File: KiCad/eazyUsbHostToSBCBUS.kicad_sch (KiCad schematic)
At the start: 23 parts, among them J1 SBC-BUS, J2 KBD_JP, J3 SERIAL, Q1 2N7000, U2 74HC04

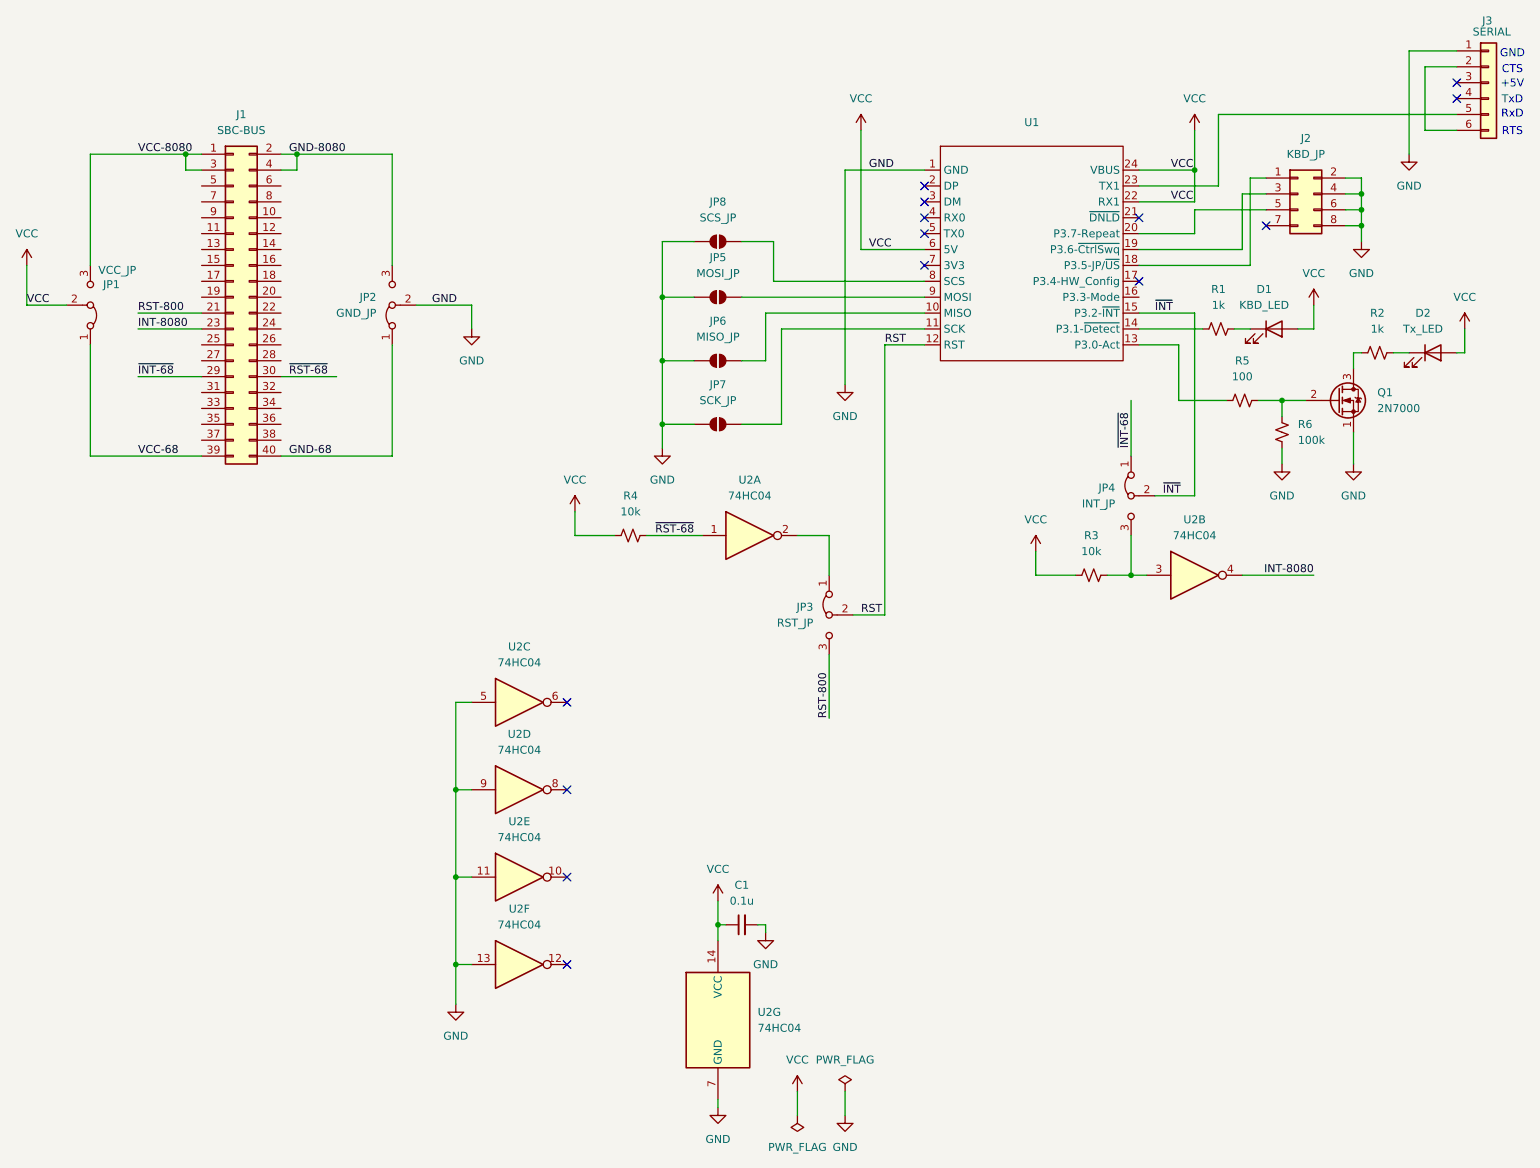
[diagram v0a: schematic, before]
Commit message: ctrl+alt+delでマイコン側へリセット信号
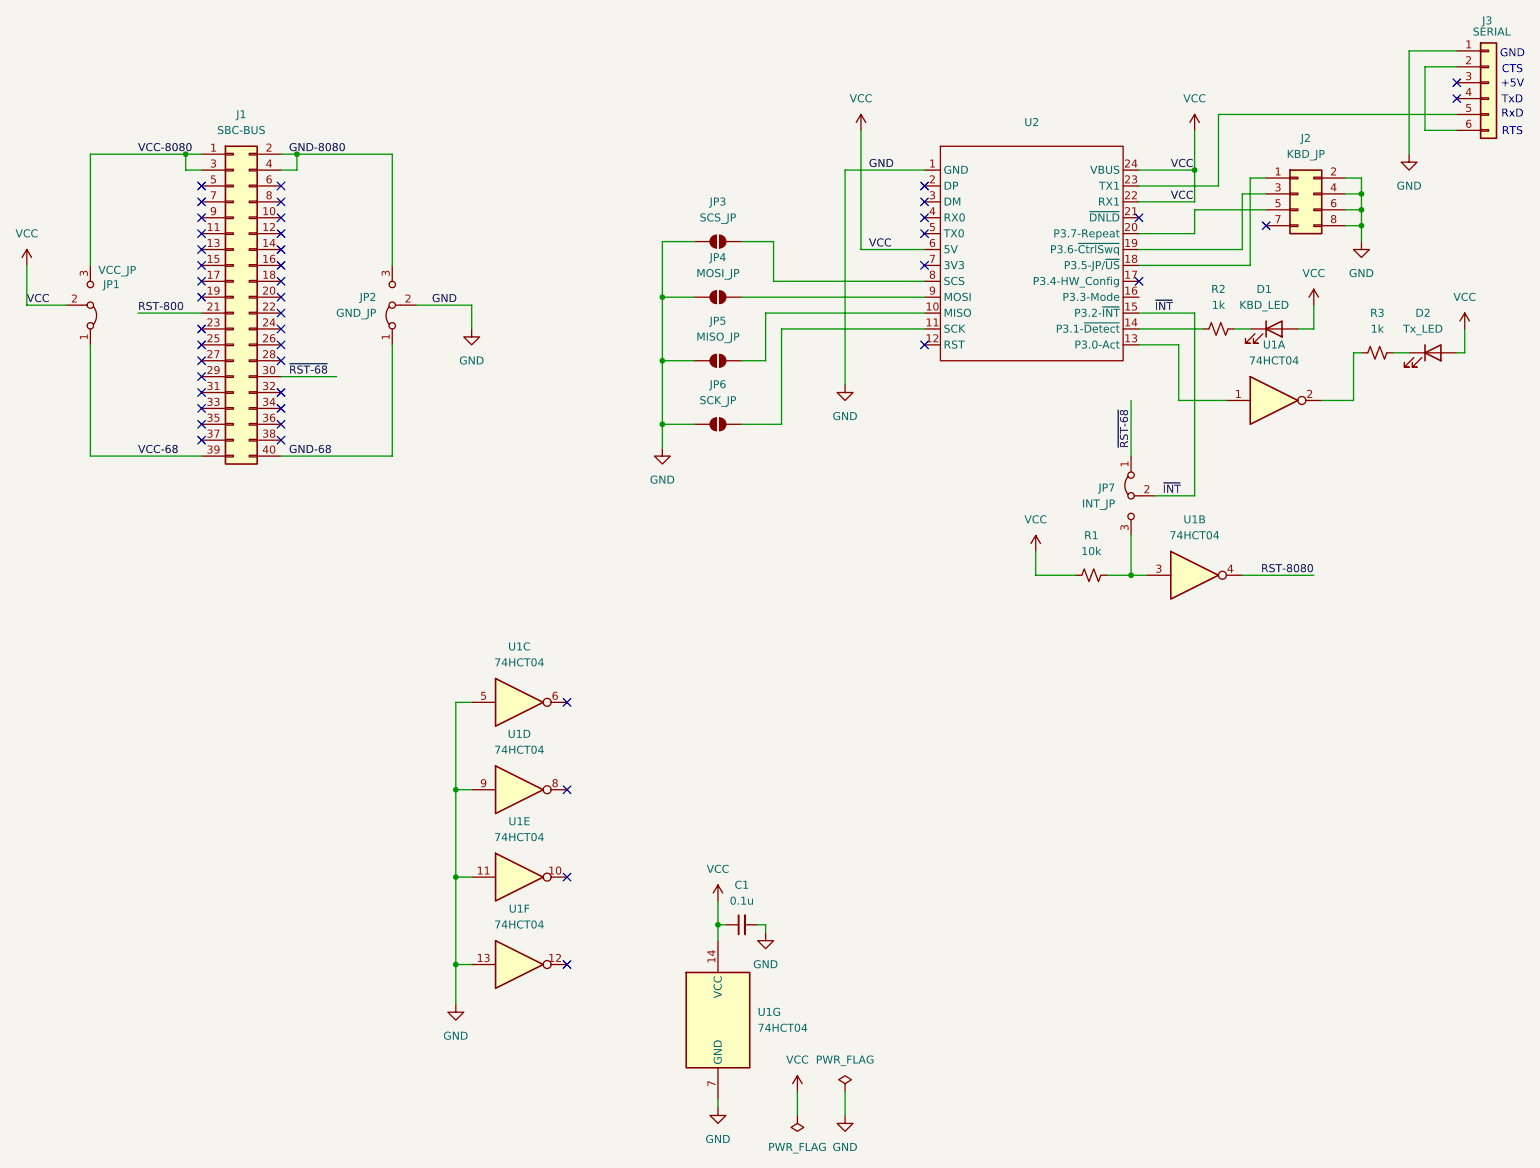
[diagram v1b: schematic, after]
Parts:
- removed JP3: RST_JP, symbol Jumper:Jumper_3_Bridged12
- removed Q1: 2N7000, Package_TO_SOT_THT:TO-92_Inline, symbol Transistor_FET:2N7000
- removed R4: 10k, symbol Device:R_Small_US
- removed R5: 100, symbol Device:R_Small_US
- removed R6: 100k, symbol Device:R_Small_US
- U1: renamed from U2; value 74HC04 -> 74HCT04
- renumbered JP8 to JP3, JP5 to JP4, JP6 to JP5, JP7 to JP6, JP4 to JP7, R3 to R1, R1 to R2, R2 to R3, U1 to U2
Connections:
- net ~{RST-68}: now also JP7.1 (A); no longer U1.1
- net at U2.13 (P3.0-Act): now also U1.1
- net at U1.2: now also R3.1
- net INT-8080: no longer names the net of J1.23 (Pin_23)
- net INT-8080: no longer U1.4
- net RST: no longer names the net of U2.12 (RST)
- net ~{INT-68}: no longer names the net of J1.29 (Pin_29)
- net ~{INT-68}: no longer JP7.1 (A)
- new net RST-8080: U1.4
- no-connect marks 14 -> 47
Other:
- moved on the sheet: U1A

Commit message: P3.2プルアップ
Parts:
- added R4: 10k, symbol Device:R_Small_US
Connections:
- net VCC: now also R4.2
- net ~{INT}: now also R4.1
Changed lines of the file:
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@@
 	)
 	(junction
+		(at 223.52 90.17)
+		(diameter 0)
+		(color 0 0 0 0)
+	)
+	(junction
 		(at 62.23 35.56)
 		(diameter 0)
@@
 	(wire
 		(pts
+			(xy 232.41 90.17) (xy 234.95 90.17)
+		)
+		(stroke
+			(width 0)
+			(type default)
+		)
+	)
+	(wire
+		(pts
 			(xy 107.95 59.69) (xy 107.95 63.5)
 		)
@@
 	(wire
 		(pts
+			(xy 223.52 90.17) (xy 227.33 90.17)
+		)
+		(stroke
+			(width 0)
+			(type default)
+		)
+	)
+	(wire
+		(pts
 			(xy 95.25 83.82) (xy 95.25 66.04)
 		)
@@
 		)
 	)
+	(wire
+		(pts
+			(xy 234.95 90.17) (xy 234.95 86.36)
+		)
+		(stroke
+			(width 0)
+			(type default)
+		)
+	)
 	(label "VCC-68"
 		(at 54.61 83.82 0)
@@
 	)
 	(symbol
+		(lib_id "power:VCC")
+		(at 234.95 86.36 0)
+		(unit 1)
+		(exclude_from_sim no)
+		(in_bom yes)
+		(on_board yes)
+		(dnp no)
+		(fields_autoplaced yes)
+		(property "Reference" "#PWR018"
+			(at 234.95 90.17 0)
+			(effects
+				(font
+					(size 1.27 1.27)
+				)
+				(hide yes)
+			)
+		)
+		(property "Value" "VCC"
+			(at 234.95 81.28 0)
+			(effects
+				(font
+					(size 1.27 1.27)
+				)
+			)
+		)
+		(property "Footprint" ""
+			(at 234.95 86.36 0)
+			(effects
+				(font
+					(size 1.27 1.27)
+				)
+				(hide yes)
+			)
+		)
+		(property "Datasheet" ""
+			(at 234.95 86.36 0)
+			(effects
+				(font
+					(size 1.27 1.27)
+				)
+				(hide yes)
+			)
+		)
+		(property "Description" "Power symbol creates a global label with name \"VCC\""
+			(at 234.95 86.36 0)
+			(effects
+				(font
+					(size 1.27 1.27)
+				)
+				(hide yes)
+			)
+		)
+		(pin "1"
+		)
+		(instances
+			(project "eazyUsbHostToSBCBUS"
+				(path "/b6e68644-57db-4ded-9351-d033555be6d6"
+					(reference "#PWR018")
+					(unit 1)
+				)
+			)
+		)
+	)
+	(symbol
 		(lib_id "74xx:74HC04")
 		(at 236.22 74.93 0)
@@
 					(unit 1)
 				)
+			)
+		)
+	)
+	(symbol
+		(lib_id "Device:R_Small_US")
+		(at 229.87 90.17 90)
+		(unit 1)
+		(exclude_from_sim no)
+		(in_bom yes)
+		(on_board yes)
+		(dnp no)
+		(fields_autoplaced yes)
+		(property "Reference" "R4"
+			(at 229.87 83.82 90)
+			(effects
+				(font
+					(size 1.27 1.27)
+				)
+			)
+		)
+		(property "Value" "10k"
+			(at 229.87 86.36 90)
+			(effects
+				(font
+					(size 1.27 1.27)
+				)
+			)
+		)
+		(property "Footprint" ""
+			(at 229.87 90.17 0)
+			(effects
+				(font
+					(size 1.27 1.27)
+				)
+				(hide yes)
+			)
+		)
+		(property "Datasheet" "~"
+			(at 229.87 90.17 0)
+			(effects
+				(font
+					(size 1.27 1.27)
+				)
+				(hide yes)
+			)
+		)
+		(property "Description" "Resistor, small US symbol"
+			(at 229.87 90.17 0)
+			(effects
+				(font
+					(size 1.27 1.27)
+				)
+				(hide yes)
+			)
+		)
+		(pin "1"
+		)
+		(pin "2"
+		)
+		(instances
+			(project "eazyUsbHostToSBCBUS"
+				(path "/b6e68644-57db-4ded-9351-d033555be6d6"
+					(reference "R4")
+					(unit 1)
+				)

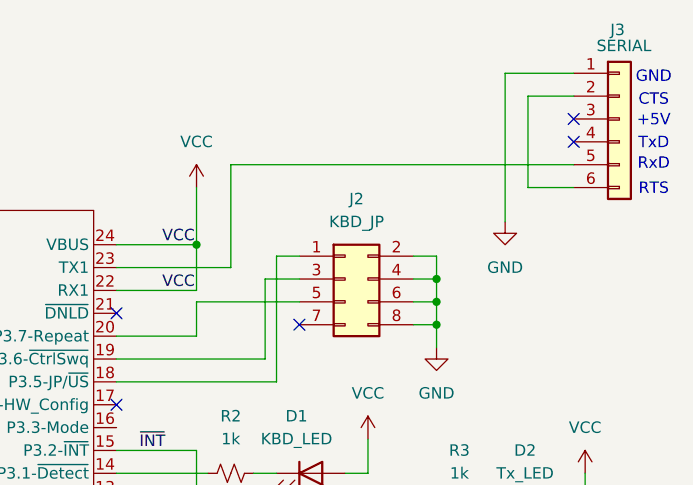
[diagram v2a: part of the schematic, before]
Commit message: 「USBかんたんホスト」CRLF初期設定PICプログラム追加
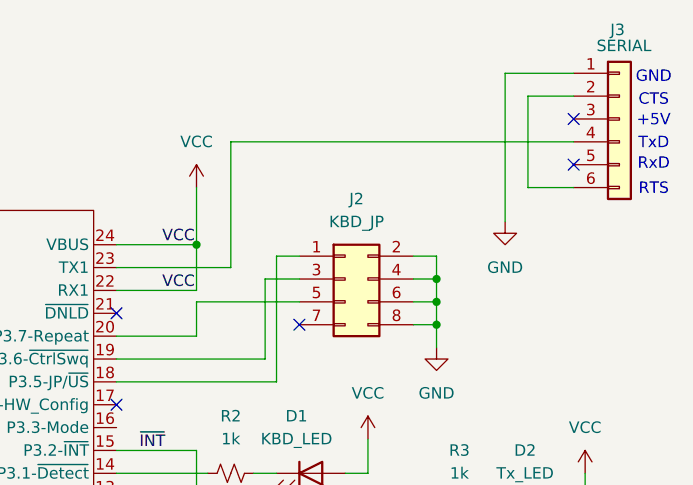
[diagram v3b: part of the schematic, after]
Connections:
- net at U2.23 (TX1): now also J3.4 (Pin_4); no longer J3.5 (Pin_5)
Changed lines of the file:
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@@
 	)
 	(no_connect
-		(at 265.43 26.67)
+		(at 265.43 29.21)
 	)
 	(no_connect
@@
 	(wire
 		(pts
-			(xy 227.33 29.21) (xy 265.43 29.21)
-		)
-		(stroke
-			(width 0)
-			(type default)
-		)
-	)
-	(wire
-		(pts
 			(xy 213.36 102.87) (xy 215.9 102.87)
 		)
@@
 	(wire
 		(pts
-			(xy 227.33 29.21) (xy 227.33 40.64)
+			(xy 227.33 26.67) (xy 227.33 40.64)
 		)
 		(stroke
@@
 		)
 		(stroke
+			(width 0)
+			(type default)
+		)
+	)
+	(wire
+		(pts
+			(xy 227.33 26.67) (xy 265.43 26.67)
+		)
+		(stroke
